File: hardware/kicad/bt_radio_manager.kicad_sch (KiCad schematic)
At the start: 26 parts, among them J1 UI module, J2 USB-C PWR A, J3 USB-C PWR B, M1 nRF24/E01-2G4M27D, M2 nRF24/E01-2G4M27D, M3 nRF24/E01-2G4M27D, M4 nRF24/E01-2G4M27D, U1 YD-ESP32-23, U2 LD1117V33

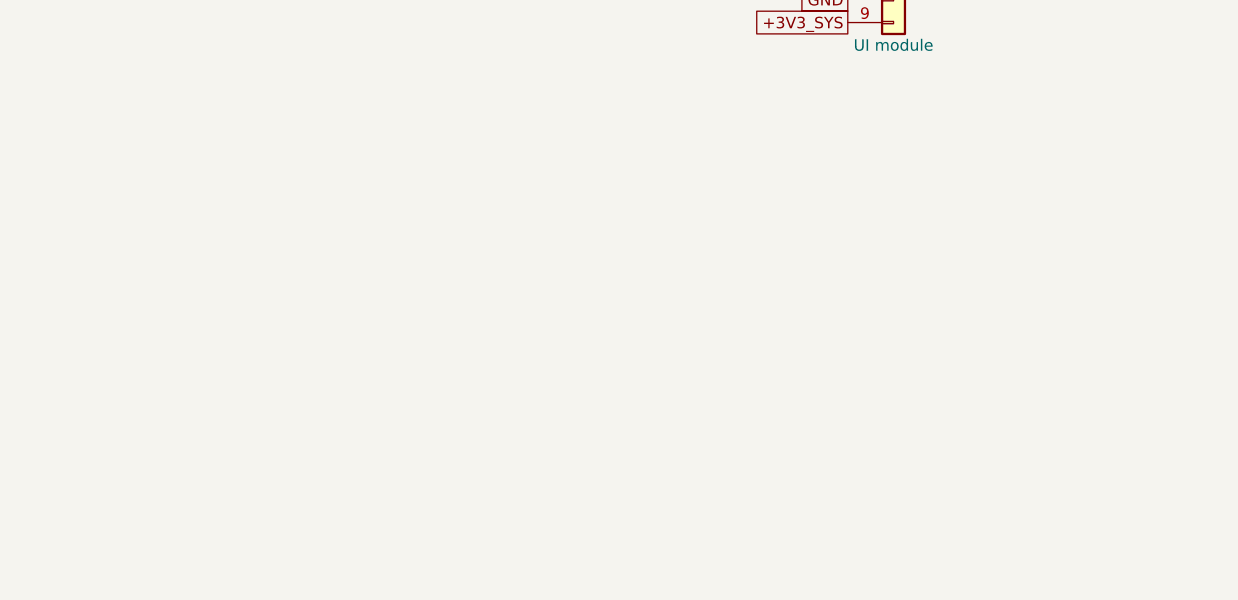
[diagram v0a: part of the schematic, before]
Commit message: Power: D2/D3 cross-feed so one 5V supply or two both work, v0.2
Two SB240 Schottkys (DO-15) join +5V_A and +5V_B in opposite
directions. With two supplies each rail runs from its own input; with
one (preferably J2) the other rail is fed through a diode. The 5V
power traces, previously 0.2 mm, are re-routed at 0.6-1.0 mm for the
~1.9 A single-supply case. Diodes placed clear of the USB-C socket
bodies (case clearance check passes for both radio variants).

Both board variants updated, gerbers and order zip re-exported,
README power section and BOM updated, version mark bumped to v0.2.

Co-Authored-By: Claude Opus 5.5 <noreply@anthropic.com>
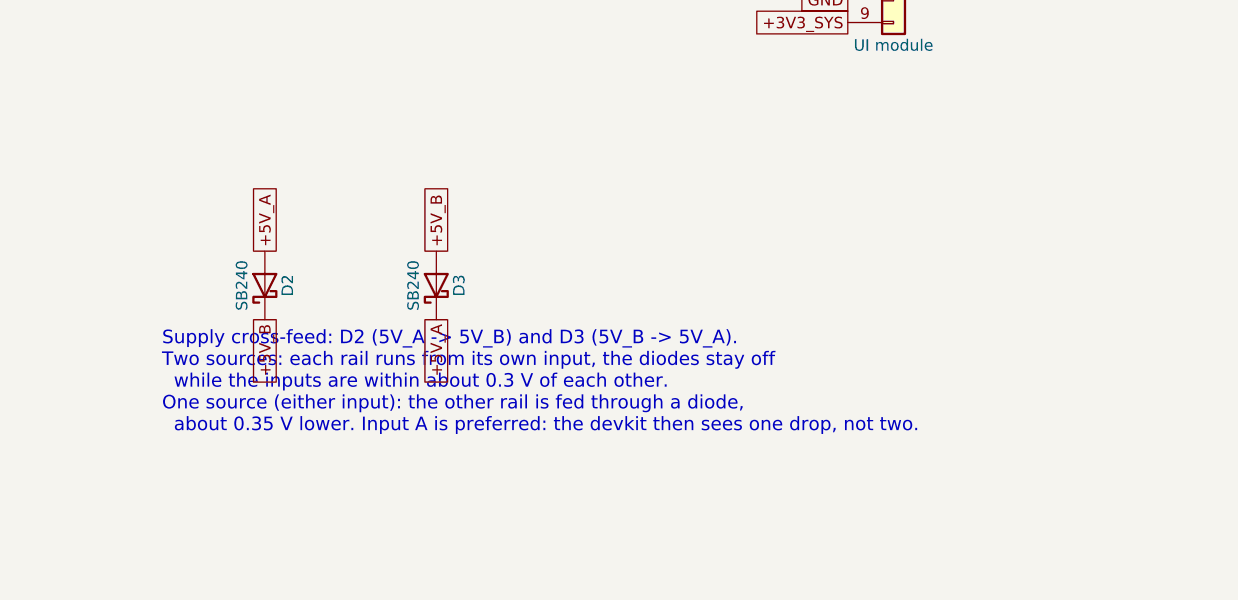
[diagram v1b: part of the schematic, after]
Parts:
- added D2, D3: SB240, Diode_THT:D_DO-15_P10.16mm_Horizontal, symbol Device:D_Schottky
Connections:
- net +5V_A: now also D2.2 (A), D3.1 (K)
- net +5V_B: now also D2.1 (K), D3.2 (A)
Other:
- note added: "Supply cross-feed: D2 (5V_A -> 5V_B) and D3 (5V_B -> 5V_A). Two sources: each rail runs from its own input, the diodes stay off while the inputs are within about 0.3 V of each other. One source (either input): the other rail is fed through a diode, about 0.35 V lower. Input A is preferred: the devkit then sees one drop, not two."
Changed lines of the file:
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@@
+		)
+	)
+	(symbol
+		(lib_id "Device:D_Schottky")
+		(at 260.35 189.23 90)
+		(unit 1)
+		(body_style 1)
+		(exclude_from_sim no)
+		(in_bom yes)
+		(on_board yes)
+		(in_pos_files yes)
+		(dnp no)
+		(property "Reference" "D2"
+			(at 262.89 189.23 0)
+			(show_name no)
+			(do_not_autoplace no)
+			(effects
+				(font
+					(size 1.27 1.27)
+				)
+			)
+		)
+		(property "Value" "SB240"
+			(at 257.81 189.23 0)
+			(show_name no)
+			(do_not_autoplace no)
+			(effects
+				(font
+					(size 1.27 1.27)
+				)
+			)
+		)
+		(property "Footprint" "Diode_THT:D_DO-15_P10.16mm_Horizontal"
+			(at 260.35 189.23 0)
+			(hide yes)
+			(show_name no)
+			(do_not_autoplace no)
+			(effects
+				(font
+					(size 1.27 1.27)
+				)
+			)
+		)
+		(property "Datasheet" ""
+			(at 260.35 189.23 0)
+			(hide yes)
+			(show_name no)
+			(do_not_autoplace no)
+			(effects
+				(font
+					(size 1.27 1.27)
+				)
+			)
+		)
+		(property "Description" "Schottky diode, 40 V 2 A"
+			(at 260.35 189.23 0)
+			(hide yes)
+			(show_name no)
+			(do_not_autoplace no)
+			(effects
+				(font
+					(size 1.27 1.27)
+				)
+			)
+		)
+		(pin "1"
+		)
+		(pin "2"
+		)
+		(instances
+			(project "bt_radio_manager"
+				(path "/759d86e3-0625-40b8-a3e4-c4e2bfc9e187"
+					(reference "D2")
+					(unit 1)
+				)
+			)
+		)
+	)
+	(global_label "+5V_A"
+		(at 260.35 185.42 90)
+		(effects
+			(font
+				(size 1.27 1.27)
+			)
+			(justify left)
+		)
+	)
+	(global_label "+5V_B"
+		(at 260.35 193.04 270)
+		(effects
+			(font
+				(size 1.27 1.27)
+			)
+			(justify right)
+		)
+	)
+	(symbol
+		(lib_id "Device:D_Schottky")
+		(at 279.4 189.23 90)
+		(unit 1)
+		(body_style 1)
+		(exclude_from_sim no)
+		(in_bom yes)
+		(on_board yes)
+		(in_pos_files yes)
+		(dnp no)
+		(property "Reference" "D3"
+			(at 281.94 189.23 0)
+			(show_name no)
+			(do_not_autoplace no)
+			(effects
+				(font
+					(size 1.27 1.27)
+				)
+			)
+		)
+		(property "Value" "SB240"
+			(at 276.86 189.23 0)
+			(show_name no)
+			(do_not_autoplace no)
+			(effects
+				(font
+					(size 1.27 1.27)
+				)
+			)
+		)
+		(property "Footprint" "Diode_THT:D_DO-15_P10.16mm_Horizontal"
+			(at 279.4 189.23 0)
+			(hide yes)
+			(show_name no)
+			(do_not_autoplace no)
+			(effects
+				(font
+					(size 1.27 1.27)
+				)
+			)
+		)
+		(property "Datasheet" ""
+			(at 279.4 189.23 0)
+			(hide yes)
+			(show_name no)
+			(do_not_autoplace no)
+			(effects
+				(font
+					(size 1.27 1.27)
+				)
+			)
+		)
+		(property "Description" "Schottky diode, 40 V 2 A"
+			(at 279.4 189.23 0)
+			(hide yes)
+			(show_name no)
+			(do_not_autoplace no)
+			(effects
+				(font
+					(size 1.27 1.27)
+				)
+			)
+		)
+		(pin "1"
+		)
+		(pin "2"
+		)
+		(instances
+			(project "bt_radio_manager"
+				(path "/759d86e3-0625-40b8-a3e4-c4e2bfc9e187"
+					(reference "D3")
+					(unit 1)
+				)
+			)
+		)
+	)
+	(global_label "+5V_B"
+		(at 279.4 185.42 90)
+		(effects
+			(font
+				(size 1.27 1.27)
+			)
+			(justify left)
+		)
+	)
+	(global_label "+5V_A"
+		(at 279.4 193.04 270)
+		(effects
+			(font
+				(size 1.27 1.27)
+			)
+			(justify right)
+		)
+	)
+	(text "Supply cross-feed: D2 (5V_A -> 5V_B) and D3 (5V_B -> 5V_A).\nTwo sources: each rail runs from its own input, the diodes stay off\n  while the inputs are within about 0.3 V of each other.\nOne source (either input): the other rail is fed through a diode,\n  about 0.35 V lower. Input A is preferred: the devkit then sees one drop, not two."
+		(exclude_from_sim no)
+		(at 248.92 205.74 0)
+		(effects
+			(font
+				(size 1.5 1.5)
+			)
+			(justify left bottom)
 		)
 	)
